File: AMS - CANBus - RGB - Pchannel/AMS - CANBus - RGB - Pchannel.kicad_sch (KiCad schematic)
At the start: 17 parts, among them J1 Power_And_CAN, J2 Screw_Terminal_01x05, Q1 IRF9Z34NPBF, Q10 2N7002, U1 LTV-817, U5 3568

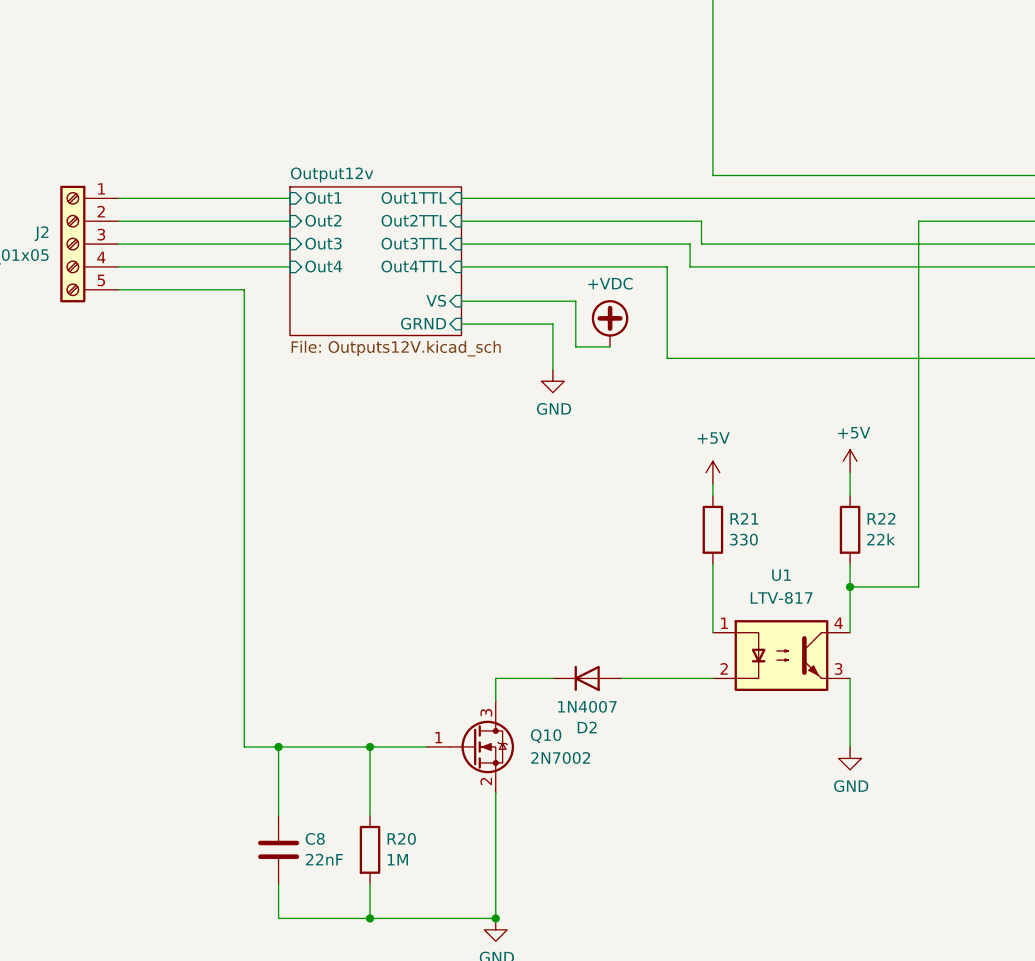
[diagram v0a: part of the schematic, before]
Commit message: RGB - PChannel V1.0 Rev A Done and routed.
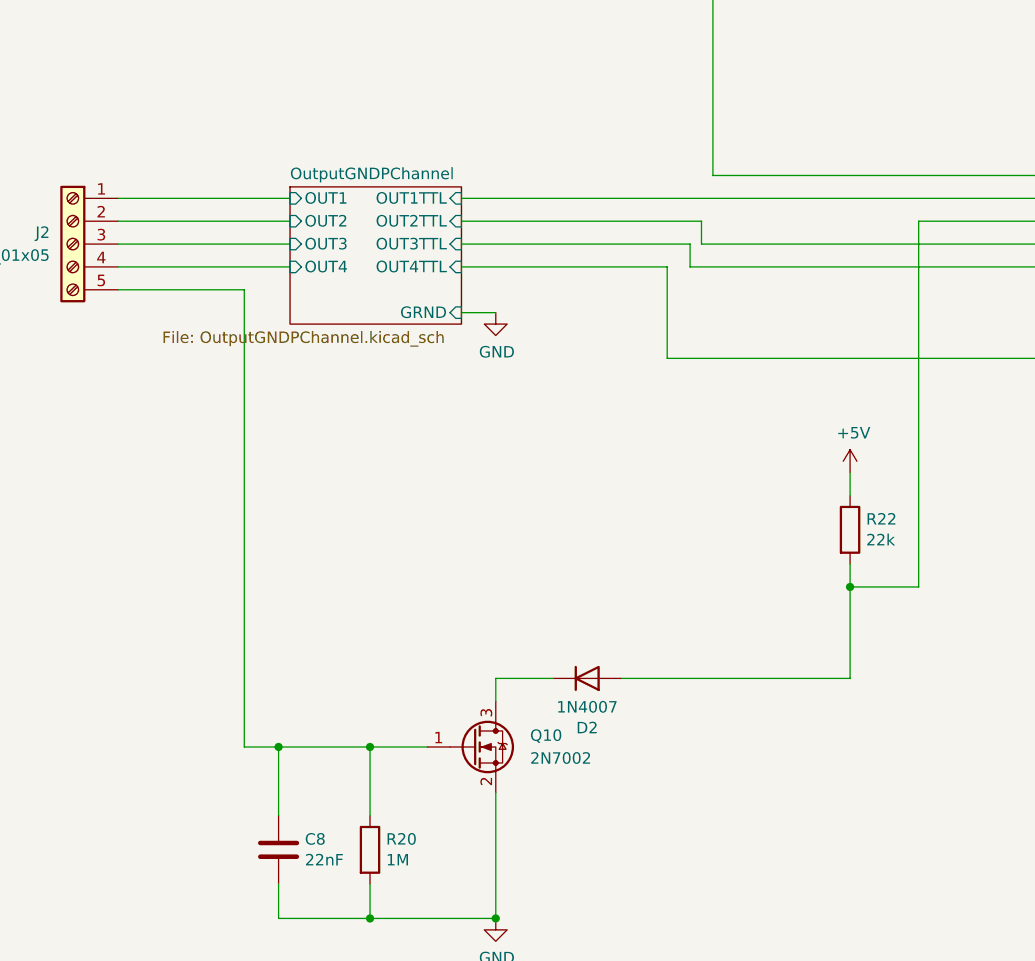
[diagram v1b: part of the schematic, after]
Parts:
- removed R21: 330, Resistor_SMD:R_1206_3216Metric_Pad1.30x1.75mm_HandSolder, symbol Device:R
- removed U1: LTV-817, Package_DIP:DIP-4_W7.62mm, symbol Isolator:LTV-817
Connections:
- net BareMinAtmel328P/PD4-D4: now also D2.2 (A)
- net Output12v/Out1 renamed OutputGNDPChannel/OUT1
- net Output12v/Out2 renamed OutputGNDPChannel/OUT2
- net Output12v/Out3 renamed OutputGNDPChannel/OUT3
- net Output12v/Out4 renamed OutputGNDPChannel/OUT4
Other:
- removed sheet Output12v
- added sheet OutputGNDPChannel (OutputGNDPChannel.kicad_sch)

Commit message: initial change from a bad low side switch to a high side switch
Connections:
- no-connect marks 8 -> 9
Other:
- sheet OutputGNDPChannel ports: added VSource; removed none
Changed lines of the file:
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@@
 (kicad_sch
-	(version 20231120)
+	(version 20250114)
 	(generator "eeschema")
-	(generator_version "8.0")
+	(generator_version "9.0")
 	(paper "A3")
 	(junction
@@
 	)
 	(no_connect
+		(at 210.82 109.22)
+	)
+	(no_connect
 		(at 266.7 135.89)
 	)
@@
 	(wire
 		(pts
-			(xy 93.98 127) (xy 97.79 127)
-		)
-		(stroke
-			(width 0)
-			(type default)
-		)
-	)
-	(wire
-		(pts
 			(xy 210.82 139.7) (xy 214.63 139.7)
 		)
@@
 	)
 	(symbol
-		(lib_id "power:GND")
-		(at 97.79 127 0)
-		(unit 1)
-		(exclude_from_sim no)
-		(in_bom yes)
-		(on_board yes)
-		(dnp no)
-		(property "Reference" "#PWR04"
-			(at 97.79 133.35 0)
-			(effects
-				(font
-					(size 1.27 1.27)
-				)
-				(hide yes)
-			)
-		)
-		(property "Value" "GND"
-			(at 97.917 131.3942 0)
-			(effects
-				(font
-					(size 1.27 1.27)
-				)
-			)
-		)
-		(property "Footprint" ""
-			(at 97.79 127 0)
-			(effects
-				(font
-					(size 1.27 1.27)
-				)
-				(hide yes)
-			)
-		)
-		(property "Datasheet" ""
-			(at 97.79 127 0)
-			(effects
-				(font
-					(size 1.27 1.27)
-				)
-				(hide yes)
-			)
-		)
-		(property "Description" ""
-			(at 97.79 127 0)
-			(effects
-				(font
-					(size 1.27 1.27)
-				)
-				(hide yes)
-			)
-		)
-		(pin "1"
-		)
-		(instances
-			(project "AMS - CANBus - RGB - Pchannel"
-				(path "/1c8b441e-37da-469b-a62d-a2093a833f7a"
-					(reference "#PWR04")
-					(unit 1)
-				)
-			)
-		)
-	)
-	(symbol
 		(lib_id "Device:C")
 		(at 73.66 186.69 0)
@@
 		(at 74.93 113.03)
 		(size 19.05 15.24)
+		(exclude_from_sim no)
+		(in_bom yes)
+		(on_board yes)
+		(dnp no)
 		(stroke
 			(width 0.1524)
@@
 			)
 		)
+		(pin "VSource" input
+			(at 93.98 124.46 0)
+			(effects
+				(font
+					(size 1.27 1.27)
+				)
+				(justify right)
+			)
+		)
 		(instances
 			(project "AMS - CANBus - RGB - Pchannel"
@@
 		(at 143.51 53.34)
 		(size 20.32 13.97)
+		(exclude_from_sim no)
+		(in_bom yes)
+		(on_board yes)
+		(dnp no)
 		(fields_autoplaced yes)
 		(stroke
@@
 		(at 143.51 27.94)
 		(size 20.32 13.97)
+		(exclude_from_sim no)
+		(in_bom yes)
+		(on_board yes)
+		(dnp no)
 		(fields_autoplaced yes)
 		(stroke
@@
 		(at 176.53 105.41)
 		(size 34.29 35.56)
+		(exclude_from_sim no)
+		(in_bom yes)
+		(on_board yes)
+		(dnp no)
 		(fields_autoplaced yes)
 		(stroke
@@
 		)
 	)
+	(embedded_fonts no)
 )
